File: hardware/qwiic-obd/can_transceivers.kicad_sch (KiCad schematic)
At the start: 15 parts, among them Q301 2N7002, U301 TH8056KDC-AAA-008-RE, U302 MCP2557FD-xMF

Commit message: OK, layout v1 complete
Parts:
- removed R301, R302, R306: 10k, Resistor_SMD:R_0805_2012Metric_Pad1.20x1.40mm_HandSolder, symbol Device:R
- renumbered R303 to R301, R304 to R302, R305 to R303, R307 to R304, R308 to R305
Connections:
- net +5V_SW renamed +5V

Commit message: Fix title block
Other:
- title: (none) -> QWIIC OBDII Interface
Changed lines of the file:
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@@
 (kicad_sch (version 20211123) (generator eeschema)
   (paper "A4")
+  (title_block
+    (title "QWIIC OBDII Interface")
+    (date "2023-01-03")
+  )
   (junction (at 176.53 60.96) (diameter 0) (color 0 0 0 0)
   )

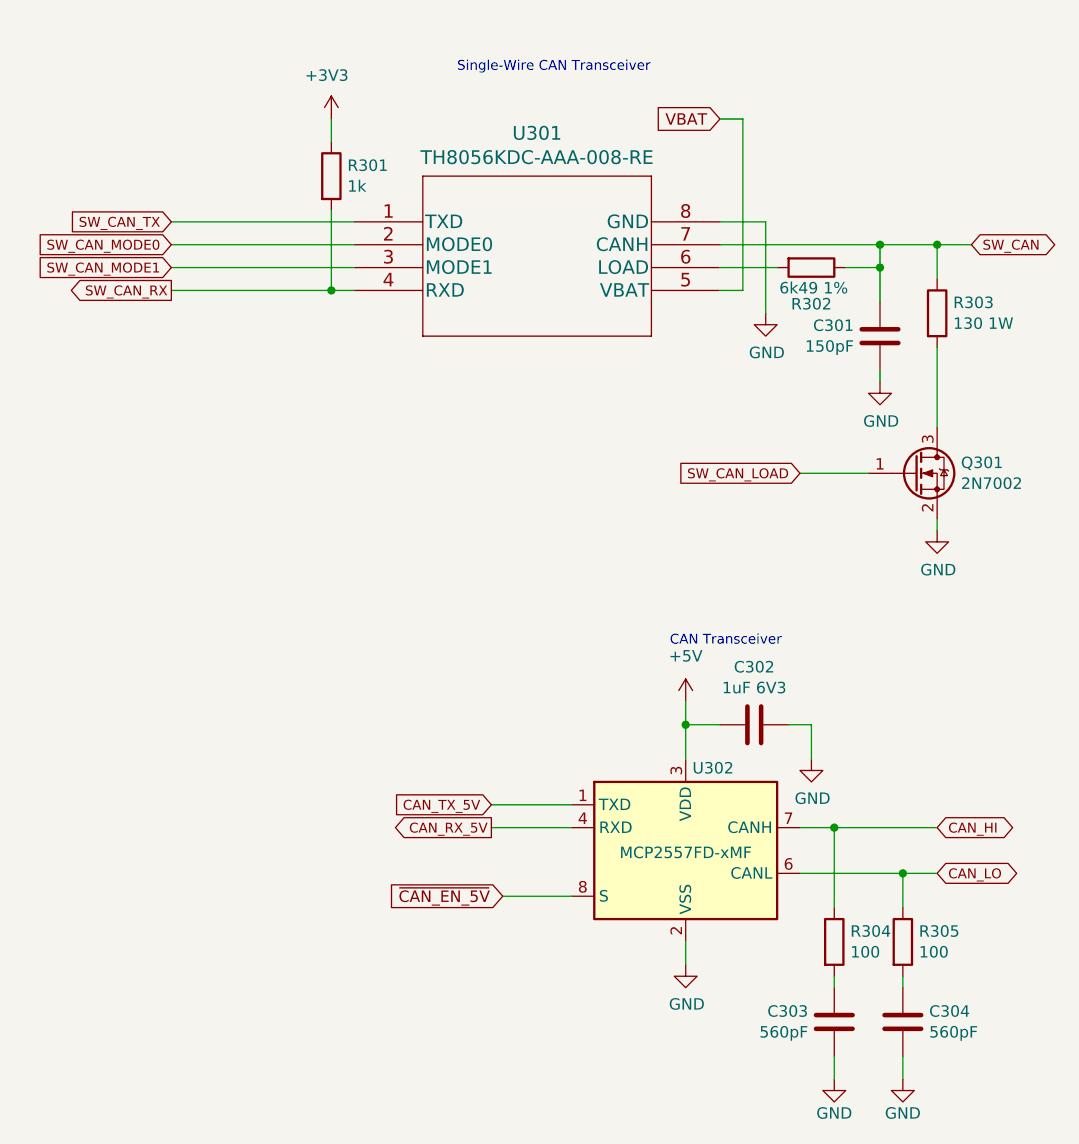
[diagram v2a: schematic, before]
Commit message: Switch out the PIC for an ATtiny424.
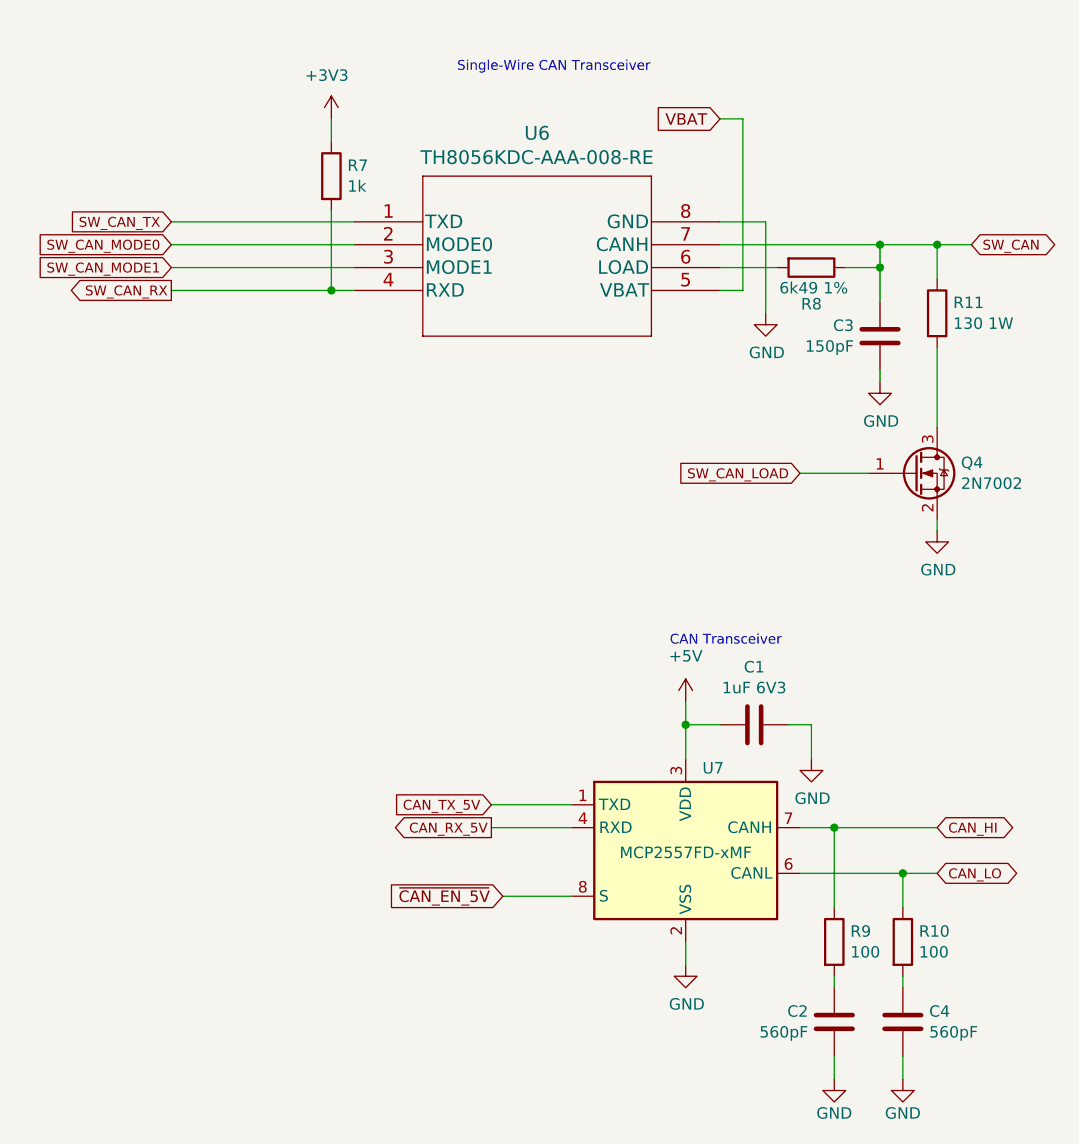
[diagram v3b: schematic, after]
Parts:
- renumbered C302 to C1, C303 to C2, C301 to C3, C304 to C4, Q301 to Q4, R305 to R10, R303 to R11, R301 to R7, R302 to R8, R304 to R9, U301 to U6, U302 to U7
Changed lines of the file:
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@@
   (symbol (lib_id "power:GND") (at 168.91 115.57 0) (unit 1)
     (in_bom yes) (on_board yes)
-    (property "Reference" "#PWR0306" (id 0) (at 168.91 121.92 0)
+    (property "Reference" "#PWR020" (id 0) (at 168.91 121.92 0)
       (effects (font (size 1.27 1.27)) hide)
     )
@@
   (symbol (lib_id "power:GND") (at 176.53 73.66 0) (unit 1)
     (in_bom yes) (on_board yes)
-    (property "Reference" "#PWR0303" (id 0) (at 176.53 80.01 0)
+    (property "Reference" "#PWR022" (id 0) (at 176.53 80.01 0)
       (effects (font (size 1.27 1.27)) hide)
     )
@@
   (symbol (lib_id "power:GND") (at 171.45 151.13 0) (unit 1)
     (in_bom yes) (on_board yes)
-    (property "Reference" "#PWR0308" (id 0) (at 171.45 157.48 0)
+    (property "Reference" "#PWR021" (id 0) (at 171.45 157.48 0)
       (effects (font (size 1.27 1.27)) hide)
     )
@@
   (symbol (lib_id "power:GND") (at 179.07 151.13 0) (unit 1)
     (in_bom yes) (on_board yes)
-    (property "Reference" "#PWR0309" (id 0) (at 179.07 157.48 0)
+    (property "Reference" "#PWR023" (id 0) (at 179.07 157.48 0)
       (effects (font (size 1.27 1.27)) hide)
     )
@@
   (symbol (lib_id "Device:R") (at 179.07 135.89 0) (unit 1)
     (in_bom yes) (on_board yes)
-    (property "Reference" "R305" (id 0) (at 180.848 134.7216 0)
+    (property "Reference" "R10" (id 0) (at 180.848 134.7216 0)
       (effects (font (size 1.27 1.27)) (justify left))
     )
@@
   (symbol (lib_id "power:+5V") (at 154.94 109.22 0) (unit 1)
     (in_bom yes) (on_board yes) (fields_autoplaced)
-    (property "Reference" "#PWR0305" (id 0) (at 154.94 113.03 0)
+    (property "Reference" "#PWR017" (id 0) (at 154.94 113.03 0)
       (effects (font (size 1.27 1.27)) hide)
     )
@@
   (symbol (lib_id "power:GND") (at 163.83 66.04 0) (unit 1)
     (in_bom yes) (on_board yes)
-    (property "Reference" "#PWR0302" (id 0) (at 163.83 72.39 0)
+    (property "Reference" "#PWR019" (id 0) (at 163.83 72.39 0)
       (effects (font (size 1.27 1.27)) hide)
     )
@@
   (symbol (lib_id "Device:C") (at 176.53 68.58 0) (mirror x) (unit 1)
     (in_bom yes) (on_board yes)
-    (property "Reference" "C301" (id 0) (at 173.6344 67.4116 0)
+    (property "Reference" "C3" (id 0) (at 173.6344 67.4116 0)
       (effects (font (size 1.27 1.27)) (justify right))
     )
@@
   (symbol (lib_id "power:+3V3") (at 115.57 44.45 0) (unit 1)
     (in_bom yes) (on_board yes)
-    (property "Reference" "#PWR0301" (id 0) (at 115.57 48.26 0)
+    (property "Reference" "#PWR016" (id 0) (at 115.57 48.26 0)
       (effects (font (size 1.27 1.27)) hide)
     )
@@
   (symbol (lib_id "Interface_CAN_LIN:MCP2557FD-xMF") (at 154.94 125.73 0) (unit 1)
     (in_bom yes) (on_board yes)
-    (property "Reference" "U302" (id 0) (at 157.988 116.586 0))
+    (property "Reference" "U7" (id 0) (at 157.988 116.586 0))
     (property "Value" "MCP2557FD-xMF" (id 1) (at 154.94 125.984 0))
     (property "Footprint" "Package_DFN_QFN:DFN-8-1EP_3x3mm_P0.65mm_EP1.55x2.4mm" (id 2) (at 154.94 140.97 0)
@@
   (symbol (lib_id "Transistor_FET:2N7002") (at 180.34 83.82 0) (unit 1)
     (in_bom yes) (on_board yes)
-    (property "Reference" "Q301" (id 0) (at 185.5216 82.6516 0)
+    (property "Reference" "Q4" (id 0) (at 185.5216 82.6516 0)
       (effects (font (size 1.27 1.27)) (justify left))
     )
@@
   (symbol (lib_id "Device:R") (at 168.91 60.96 270) (unit 1)
     (in_bom yes) (on_board yes)
-    (property "Reference" "R302" (id 0) (at 168.91 65.024 90))
+    (property "Reference" "R8" (id 0) (at 168.91 65.024 90))
     (property "Value" "6k49 1%" (id 1) (at 169.164 63.246 90))
     (property "Footprint" "Resistor_SMD:R_0805_2012Metric_Pad1.20x1.40mm_HandSolder" (id 2) (at 168.91 59.182 90)
@@
   (symbol (lib_id "Device:R") (at 182.88 66.04 0) (unit 1)
     (in_bom yes) (on_board yes)
-    (property "Reference" "R303" (id 0) (at 184.658 64.8716 0)
+    (property "Reference" "R11" (id 0) (at 184.658 64.8716 0)
       (effects (font (size 1.27 1.27)) (justify left))
     )
@@
   (symbol (lib_id "Device:C") (at 162.56 111.76 270) (unit 1)
     (in_bom yes) (on_board yes)
-    (property "Reference" "C302" (id 0) (at 162.56 105.3592 90))
+    (property "Reference" "C1" (id 0) (at 162.56 105.3592 90))
     (property "Value" "1uF 6V3" (id 1) (at 162.56 107.6706 90))
     (property "Footprint" "Capacitor_SMD:C_0805_2012Metric_Pad1.18x1.45mm_HandSolder" (id 2) (at 158.75 112.7252 0)
@@
   (symbol (lib_id "UltraLibrarian:TH8056KDC-AAA-008-RE") (at 118.11 55.88 0) (unit 1)
     (in_bom yes) (on_board yes)
-    (property "Reference" "U301" (id 0) (at 138.43 46.0502 0)
+    (property "Reference" "U6" (id 0) (at 138.43 46.0502 0)
       (effects (font (size 1.524 1.524)))
     )
@@
   (symbol (lib_id "Device:R") (at 171.45 135.89 0) (unit 1)
     (in_bom yes) (on_board yes)
-    (property "Reference" "R304" (id 0) (at 173.228 134.7216 0)
+    (property "Reference" "R9" (id 0) (at 173.228 134.7216 0)
       (effects (font (size 1.27 1.27)) (justify left))
     )
@@
   (symbol (lib_id "power:GND") (at 182.88 90.17 0) (unit 1)
     (in_bom yes) (on_board yes)
-    (property "Reference" "#PWR0304" (id 0) (at 182.88 96.52 0)
+    (property "Reference" "#PWR024" (id 0) (at 182.88 96.52 0)
       (effects (font (size 1.27 1.27)) hide)
     )
@@
   (symbol (lib_id "Device:R") (at 115.57 50.8 0) (unit 1)
     (in_bom yes) (on_board yes)
-    (property "Reference" "R301" (id 0) (at 117.348 49.6316 0)
+    (property "Reference" "R7" (id 0) (at 117.348 49.6316 0)
       (effects (font (size 1.27 1.27)) (justify left))
     )
@@
   (symbol (lib_id "Device:C") (at 179.07 144.78 0) (unit 1)
     (in_bom yes) (on_board yes)
-    (property "Reference" "C304" (id 0) (at 181.991 143.6116 0)
+    (property "Reference" "C4" (id 0) (at 181.991 143.6116 0)
       (effects (font (size 1.27 1.27)) (justify left))
     )
@@
   (symbol (lib_id "power:GND") (at 154.94 138.43 0) (unit 1)
     (in_bom yes) (on_board yes)
-    (property "Reference" "#PWR0307" (id 0) (at 154.94 144.78 0)
+    (property "Reference" "#PWR018" (id 0) (at 154.94 144.78 0)
       (effects (font (size 1.27 1.27)) hide)
     )
@@
   (symbol (lib_id "Device:C") (at 171.45 144.78 0) (mirror x) (unit 1)
     (in_bom yes) (on_board yes)
-    (property "Reference" "C303" (id 0) (at 168.5544 143.6116 0)
+    (property "Reference" "C2" (id 0) (at 168.5544 143.6116 0)
       (effects (font (size 1.27 1.27)) (justify right))
     )
